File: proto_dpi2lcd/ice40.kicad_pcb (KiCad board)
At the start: 4 copper layers, 50 x 50 mm, 42 parts, among them J101 Conn_02x05_Odd_Even, J6 Conn_01x40_MountingPin, U1 ASDMB-xxxMHz, U102 iCE40HX1K-CB132, U103 W25Q32JVSS, U104 TLV71312PDBV, U105 TLV71325PDBV

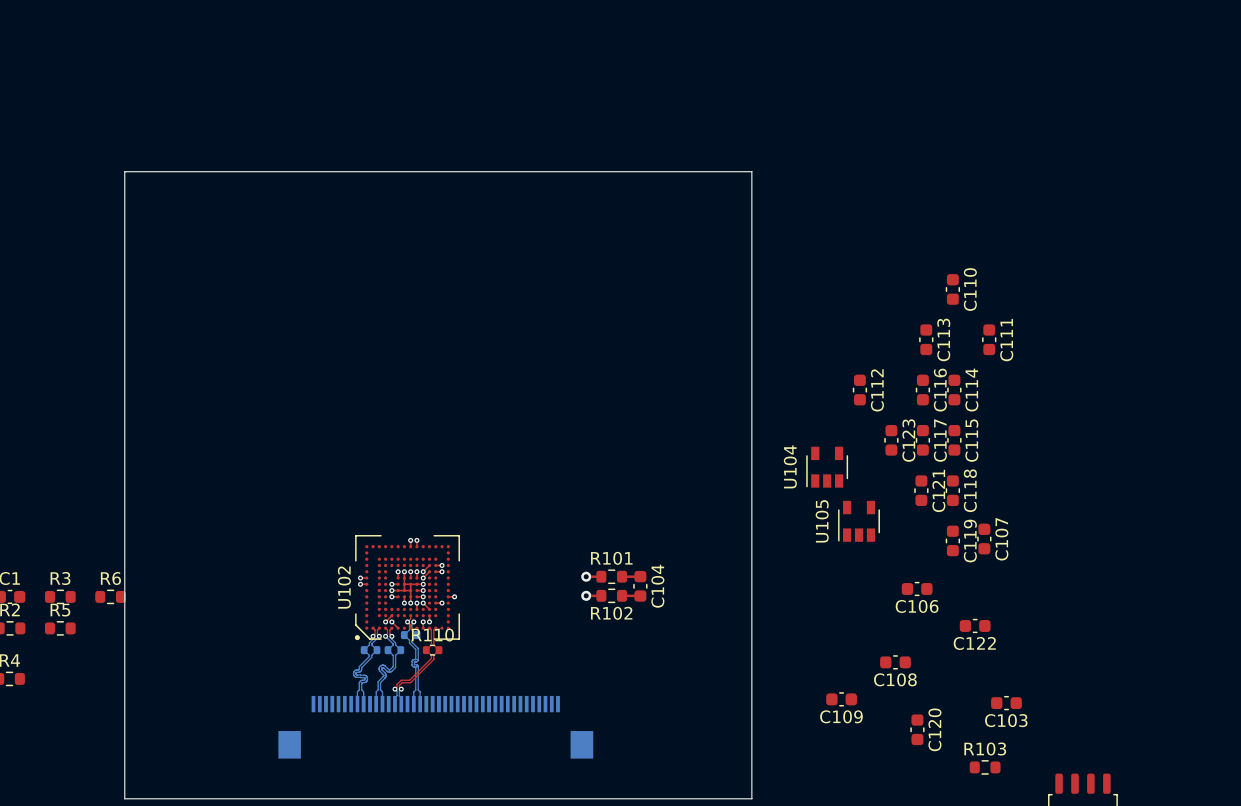
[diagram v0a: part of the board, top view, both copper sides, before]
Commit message: Work in progress
- Schematic of 12V to 3,3V BUCK
 - pin allocation from RPi header to FPGA
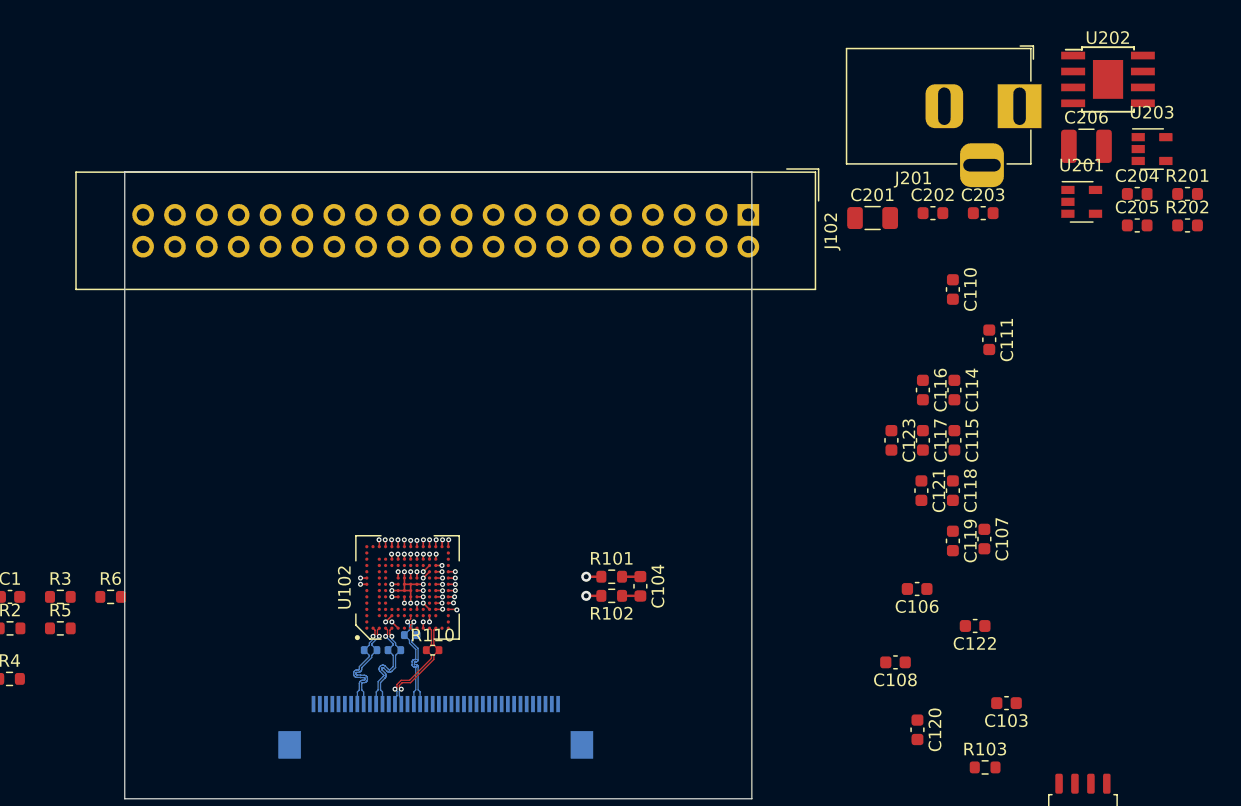
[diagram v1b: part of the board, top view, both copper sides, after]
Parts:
- removed C109, C112, C113: 100n, Capacitor_SMD:C_0603_1608Metric
- removed U104: TLV71312PDBV, Package_TO_SOT_SMD:SOT-23-5
- removed U105: TLV71325PDBV, Package_TO_SOT_SMD:SOT-23-5
- added C201: 4u7, Capacitor_SMD:C_1206_3216Metric, F.Cu at (182.9, 83.9)
- added C202: 100n, Capacitor_SMD:C_0603_1608Metric, F.Cu at (187.7, 83.6)
- added C203: 100n, Capacitor_SMD:C_0603_1608Metric, F.Cu at (191.7, 83.6)
- added C204: 100n, Capacitor_SMD:C_0603_1608Metric, F.Cu at (204.0, 82.0)
- added C205: 100n, Capacitor_SMD:C_0603_1608Metric, F.Cu at (204.0, 84.5)
- added C206: 22u, Capacitor_SMD:C_1210_3225Metric, F.Cu at (199.9, 78.2)
- added J102: Raspberry_Pi_2_3, Connector_IDC:IDC-Header_2x20_P2.54mm_Vertical, F.Cu at (173.0, 83.7)
- added J201: Barrel_Jack_Switch, Connector_BarrelJack:BarrelJack_Horizontal, F.Cu at (194.6, 75.0)
- added R201: 47k, Resistor_SMD:R_0603_1608Metric, F.Cu at (208.0, 82.0)
- added R202: 150k, Resistor_SMD:R_0603_1608Metric, F.Cu at (208.0, 84.5)
- added U201: TLV71325PDBV, Package_TO_SOT_SMD:SOT-23-5, F.Cu at (199.6, 82.7)
- added U202: ST1S10PHR, Package_SO:TI_SO-PowerPAD-8, F.Cu at (201.7, 72.9)
- added U203: TLV71312PDBV, Package_TO_SOT_SMD:SOT-23-5, F.Cu at (205.2, 78.4)
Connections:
- net /24 renamed Net-(U102-PadM3)
- net /25 renamed Net-(U102-PadL4)
- net /26 renamed Net-(U102-PadP2)
- net /27 renamed Net-(U102-PadP3)
- net /29 renamed Net-(U102-PadL5)
- net /31 renamed Net-(U102-PadL6)
- net /38 renamed Net-(U102-PadL7)
- net /40 renamed Net-(U102-PadL8)
- net /42 renamed Net-(U102-PadL9)
- J6 pad 38: +3V3 -> /VCCS
- J6 pad 39: +3V3 -> /VCCS
- U102 pad C14: Net-(U102-PadC14) -> /R1
- U102 pad D14: Net-(U102-PadD14) -> /R0
- U102 pad E12: Net-(U102-PadE12) -> /R6
- U102 pad E14: Net-(U102-PadE14) -> /G4
- U102 pad F12: Net-(U102-PadF12) -> /G7
- U102 pad F14: Net-(U102-PadF14) -> /G1
- U102 pad G12: Net-(U102-PadG12) -> /G0
- U102 pad G14: Net-(U102-PadG14) -> /B2
- U102 pad H12: Net-(U102-PadH12) -> /B1
- U102 pad J12: Net-(U102-PadJ12) -> /DEN
- U102 pad K12: Net-(U102-PadK12) -> /CLK
- U102 pad K14: Net-(U102-PadK14) -> /B3
- U102 pad L12: Net-(U102-PadL12) -> /B4
- U102 pad L14: Net-(U102-PadL14) -> /B7
- U102 pad M12: Net-(U102-PadM12) -> /R5
- U102 pad M4: /28 -> /V_SYNC
- U102 pad M6: /33 -> /G2
- U102 pad M7: /34 -> /G3
- U102 pad M8: /39 -> /G6
- U102 pad M9: /41 -> /R2
- U102 pad N14: Net-(U102-PadN14) -> /B5
- U102 pad P10: /43 -> /R4
- U102 pad P14: Net-(U102-PadP14) -> /B6
- U102 pad P4: /30 -> /H_SYNC
- U102 pad P5: /32 -> /B0
- U102 pad P7: /35 -> /G5
- U102 pad P8: /36 -> /R7
- U102 pad P9: /37 -> /R3
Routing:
- net /H_SYNC: track 0.00 -> 0.70 mm, vias 0 -> 1
- net /B5: track 0.00 -> 0.57 mm, vias 0 -> 1
- net /R0: track 0.00 -> 0.56 mm, vias 0 -> 1
- net Net-(U102-PadM14): track 0.00 -> 0.56 mm, vias 0 -> 1
- net /B6: track 0.00 -> 0.56 mm, vias 0 -> 1
- net /R4: track 0.00 -> 0.56 mm, vias 0 -> 1
- net /G4: track 0.00 -> 0.56 mm, vias 0 -> 1
- net /R7: track 0.00 -> 0.56 mm, vias 0 -> 1
- net /R1: track 0.00 -> 0.56 mm, vias 0 -> 1
- net /G5: track 0.00 -> 0.56 mm, vias 0 -> 1
- net /R3: track 0.00 -> 0.56 mm, vias 0 -> 1
- net /G1: track 0.00 -> 0.56 mm, vias 0 -> 1
- net /B3: track 0.00 -> 0.56 mm, vias 0 -> 1
- net /V_SYNC: track 0.00 -> 0.55 mm, vias 0 -> 1
- net /B2: track 0.00 -> 0.55 mm, vias 0 -> 1
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
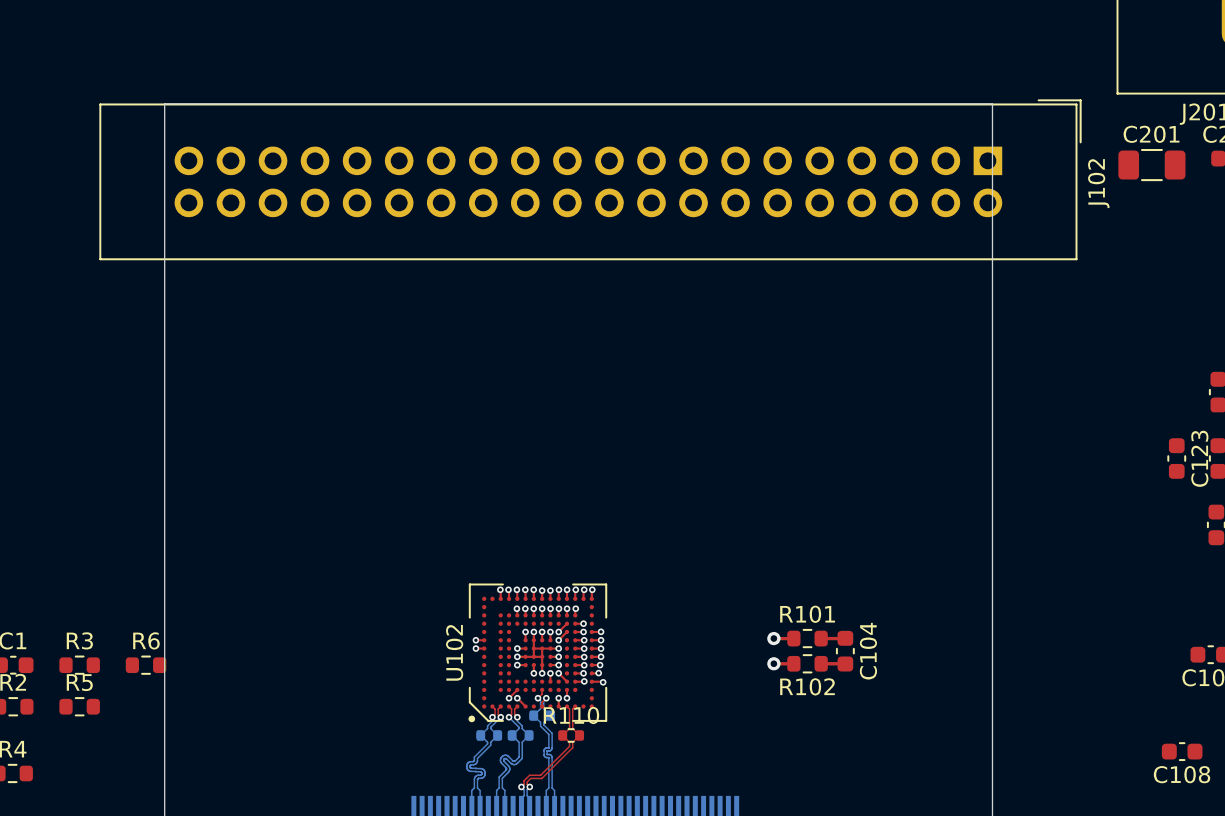
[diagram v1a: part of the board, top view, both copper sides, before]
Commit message: Fanout of DPI
(Display Parallel Interface)
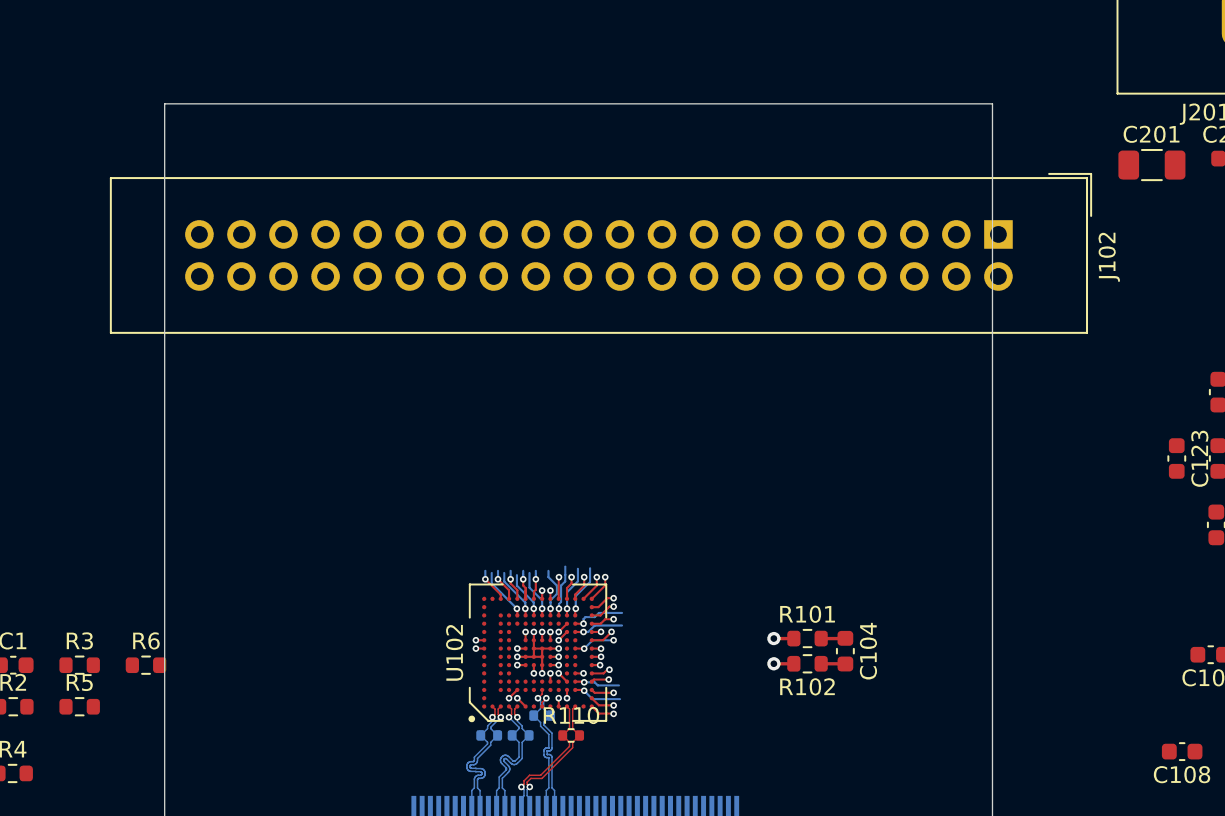
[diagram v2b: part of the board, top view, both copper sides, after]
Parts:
- moved J102 4.49 mm to (173.6, 88.1)
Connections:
- J101 pad 3: Net-(J101-Pad3) -> (no net)
- J101 pad 4: Net-(J101-Pad4) -> (no net)
- J102 pad 1: Net-(J102-Pad1) -> (no net)
- J102 pad 17: Net-(J102-Pad17) -> (no net)
- J102 pad 2: Net-(J102-Pad2) -> (no net)
- J102 pad 4: Net-(J102-Pad4) -> (no net)
- J201 pad 3: Net-(J201-Pad3) -> (no net)
- J6 pad 11: Net-(J6-Pad11) -> (no net)
- J6 pad 12: Net-(J6-Pad12) -> (no net)
- J6 pad 14: Net-(J6-Pad14) -> (no net)
- J6 pad 15: Net-(J6-Pad15) -> (no net)
- J6 pad 17: Net-(J6-Pad17) -> (no net)
- J6 pad 18: Net-(J6-Pad18) -> (no net)
- J6 pad 20: Net-(J6-Pad20) -> (no net)
- J6 pad 21: Net-(J6-Pad21) -> (no net)
- J6 pad 34: /DATA_EDID -> (no net)
- J6 pad 35: /CLK_EDID -> (no net)
- J6 pad 36: Net-(J6-Pad36) -> (no net)
- J6 pad 37: /VEDID -> (no net)
- J6 pad 4: Net-(J6-Pad4) -> (no net)
- J6 pad 40: Net-(J6-Pad40) -> (no net)
- J6 pad 5: /LED_EN -> (no net)
- J6 pad 6: /LED_PWM -> (no net)
- J6 pad 7: Net-(J6-Pad7) -> (no net)
- U1 pad 3: /CLOCK -> (no net)
- U102 pad A1: Net-(U102-PadA1) -> (no net)
- U102 pad A10: Net-(U102-PadA10) -> (no net)
- U102 pad A11: Net-(U102-PadA11) -> (no net)
- U102 pad A12: Net-(U102-PadA12) -> (no net)
- U102 pad A13: Net-(U102-PadA13) -> (no net)
- U102 pad A2: Net-(U102-PadA2) -> (no net)
- U102 pad A3: Net-(U102-PadA3) -> (no net)
- U102 pad A4: Net-(U102-PadA4) -> (no net)
- U102 pad A5: Net-(U102-PadA5) -> (no net)
- U102 pad A6: Net-(U102-PadA6) -> (no net)
- U102 pad A7: Net-(U102-PadA7) -> (no net)
- U102 pad B14: Net-(U102-PadB14) -> (no net)
- U102 pad C10: Net-(U102-PadC10) -> (no net)
- U102 pad C11: Net-(U102-PadC11) -> (no net)
- U102 pad C12: Net-(U102-PadC12) -> (no net)
- U102 pad C3: Net-(U102-PadC3) -> (no net)
- U102 pad C4: Net-(U102-PadC4) -> (no net)
- U102 pad C5: Net-(U102-PadC5) -> (no net)
- U102 pad C6: Net-(U102-PadC6) -> (no net)
- U102 pad C7: Net-(U102-PadC7) -> (no net)
- U102 pad C8: Net-(U102-PadC8) -> (no net)
- U102 pad C9: Net-(U102-PadC9) -> (no net)
- U102 pad D10: Net-(U102-PadD10) -> (no net)
- U102 pad D11: Net-(U102-PadD11) -> (no net)
- U102 pad D12: Net-(U102-PadD12) -> (no net)
- U102 pad D3: Net-(U102-PadD3) -> (no net)
- U102 pad D4: Net-(U102-PadD4) -> (no net)
- U102 pad D5: Net-(U102-PadD5) -> (no net)
- U102 pad D6: Net-(U102-PadD6) -> (no net)
- U102 pad D7: Net-(U102-PadD7) -> (no net)
- U102 pad D8: Net-(U102-PadD8) -> (no net)
- U102 pad D9: Net-(U102-PadD9) -> (no net)
- U102 pad E11: Net-(U102-PadE11) -> (no net)
- U102 pad E4: Net-(U102-PadE4) -> (no net)
- U102 pad F11: Net-(U102-PadF11) -> (no net)
- U102 pad F3: Net-(U102-PadF3) -> (no net)
- U102 pad F4: Net-(U102-PadF4) -> (no net)
- U102 pad G1: Net-(U102-PadG1) -> (no net)
- U102 pad G11: Net-(U102-PadG11) -> (no net)
- U102 pad G3: Net-(U102-PadG3) -> (no net)
- U102 pad G4: Net-(U102-PadG4) -> (no net)
- U102 pad H11: Net-(U102-PadH11) -> (no net)
- U102 pad H4: Net-(U102-PadH4) -> (no net)
- U102 pad J1: Net-(U102-PadJ1) -> (no net)
- U102 pad J11: Net-(U102-PadJ11) -> (no net)
- U102 pad J3: Net-(U102-PadJ3) -> (no net)
- U102 pad K11: Net-(U102-PadK11) -> (no net)
- U102 pad K3: Net-(U102-PadK3) -> (no net)
- U102 pad K4: Net-(U102-PadK4) -> (no net)
- U102 pad L4: Net-(U102-PadL4) -> (no net)
- U102 pad L5: Net-(U102-PadL5) -> (no net)
- U102 pad L6: Net-(U102-PadL6) -> (no net)
- U102 pad L7: Net-(U102-PadL7) -> (no net)
- U102 pad L8: Net-(U102-PadL8) -> (no net)
- U102 pad L9: Net-(U102-PadL9) -> (no net)
- U102 pad M14: Net-(U102-PadM14) -> (no net)
- U102 pad M3: Net-(U102-PadM3) -> /B0
- U102 pad M4: /V_SYNC -> /G3
- U102 pad M6: /G2 -> (no net)
- U102 pad M7: /G3 -> (no net)
- U102 pad M8: /G6 -> /R7
- U102 pad M9: /R2 -> (no net)
- U102 pad P2: Net-(U102-PadP2) -> /V_SYNC
- U102 pad P3: Net-(U102-PadP3) -> /H_SYNC
- U102 pad P4: /H_SYNC -> /G2
- U102 pad P5: /B0 -> /G5
- U102 pad P7: /G5 -> /G6
- U102 pad P8: /R7 -> /R2
- U201 pad 4: Net-(U201-Pad4) -> (no net)
- U202 pad 7: Net-(L201-Pad1) -> (no net)
- U203 pad 4: Net-(U203-Pad4) -> (no net)
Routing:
- net /R5: track 0.42 -> 3.22 mm
- net /R6: track 0.42 -> 3.21 mm
- net /SDO: track 0.50 -> 3.26 mm
- net /CLK: track 0.41 -> 3.11 mm
- net /G7: track 0.41 -> 3.11 mm
- net /B4: track 0.41 -> 3.09 mm
- net /DEN: track 0.41 -> 3.06 mm
- net /B0: track 0.42 -> 2.93 mm
- net /CDONE: track 0.50 -> 2.99 mm
- net /B1: track 0.41 -> 2.88 mm
- net /G0: track 0.41 -> 2.86 mm
- net (no net): track 0.00 -> 2.24 mm, vias 0 -> 2
- net /G3: track 0.55 -> 2.73 mm
- net /R7: track 0.56 -> 2.53 mm, vias 1 -> 2
- net /G1: track 0.56 -> 2.28 mm
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
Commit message: Progressing
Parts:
- removed the C107 at (191.8, 109.5)
- removed the C111 at (192.2, 93.7)
- added C104: 100n, Capacitor_SMD:C_0402_1005Metric, B.Cu at (147.8, 113.2)
- added C109: 100n, Capacitor_SMD:C_0402_1005Metric, B.Cu at (145.0, 115.4)
- added D102: Green, Diode_SMD:D_0805_2012Metric, F.Cu at (215.1, 118.1)
- added D103: Green, Diode_SMD:D_0805_2012Metric, F.Cu at (219.6, 118.1)
- added D201: Green, Diode_SMD:D_0805_2012Metric, F.Cu at (198.1, 106.8)
- added D202: P6SMBJ15A, Diode_SMD:D_SMB, F.Cu at (200.0, 102.5)
- added R114: 200R, Resistor_SMD:R_0603_1608Metric, F.Cu at (214.9, 120.9)
- added R115: 200R, Resistor_SMD:R_0603_1608Metric, F.Cu at (236.0, 109.3)
- added R116: 10k, Resistor_SMD:R_0603_1608Metric, F.Cu at (218.9, 120.9)
- added R117: 10k, Resistor_SMD:R_0603_1608Metric, F.Cu at (223.8, 117.8)
- added R201: 200R, Resistor_SMD:R_0603_1608Metric, F.Cu at (206.2, 105.2)
- added SW101: SW1, Button_Switch_THT:SW_PUSH_6mm_H4.3mm, F.Cu at (214.9, 110.1)
- added SW102: SW2, Button_Switch_THT:SW_PUSH_6mm_H4.3mm, F.Cu at (225.5, 110.1)
- C106: footprint Capacitor_SMD:C_0603_1608Metric -> Capacitor_SMD:C_0402_1005Metric; moved to B.Cu
- C107: renamed from C108; footprint Capacitor_SMD:C_0603_1608Metric -> Capacitor_SMD:C_0402_1005Metric; moved to B.Cu
- C108: renamed from C110; footprint Capacitor_SMD:C_0603_1608Metric -> Capacitor_SMD:C_0402_1005Metric; moved to B.Cu
- C201: value 4u7 -> 10u/35V; footprint Capacitor_SMD:C_1206_3216Metric -> Capacitor_SMD:C_1210_3225Metric
- C206: value 22u -> 22u/25V
- U103: renamed from U1; value ASDMB-xxxMHz -> 520-2520MVLC-400BNTR
- moved C108 49.8 mm to (145.8, 113.9), turned to 0 degrees
- moved C107 41.4 mm to (143.8, 113.2), turned to 90 degrees
- moved C106 40.6 mm to (145.8, 112.9), turned to 0 degrees
- moved C105 30.3 mm to (157.1, 103.4)
- moved C201 30.0 mm to (207.0, 101.9)
- renumbered C114 to C101, C104 to C102, C115 to C103, C116 to C105, C103 to C110, C1 to C111, C120 to C112, C121 to C113, C117 to C114, C118 to C115, C119 to C116, C122 to C117, C123 to C118, D1 to D101, J6 to J101, J101 to J103, R105 to R102, R106 to R103, R102 to R104, R110 to R105, R108 to R106, R1 to R107, R2 to R108, R3 to R109, R4 to R110, R5 to R111, R103 to R112, R6 to R113, R201 to R202, R202 to R203, U102 to U101, U103 to U102
